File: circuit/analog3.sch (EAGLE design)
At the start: 67 parts, among them IC1 OP07C, IC2 74HC4052D, IC3 AD8603UJ, IC4 AD8221R, IC5 AD8221R, IC6 AD8532ARZ

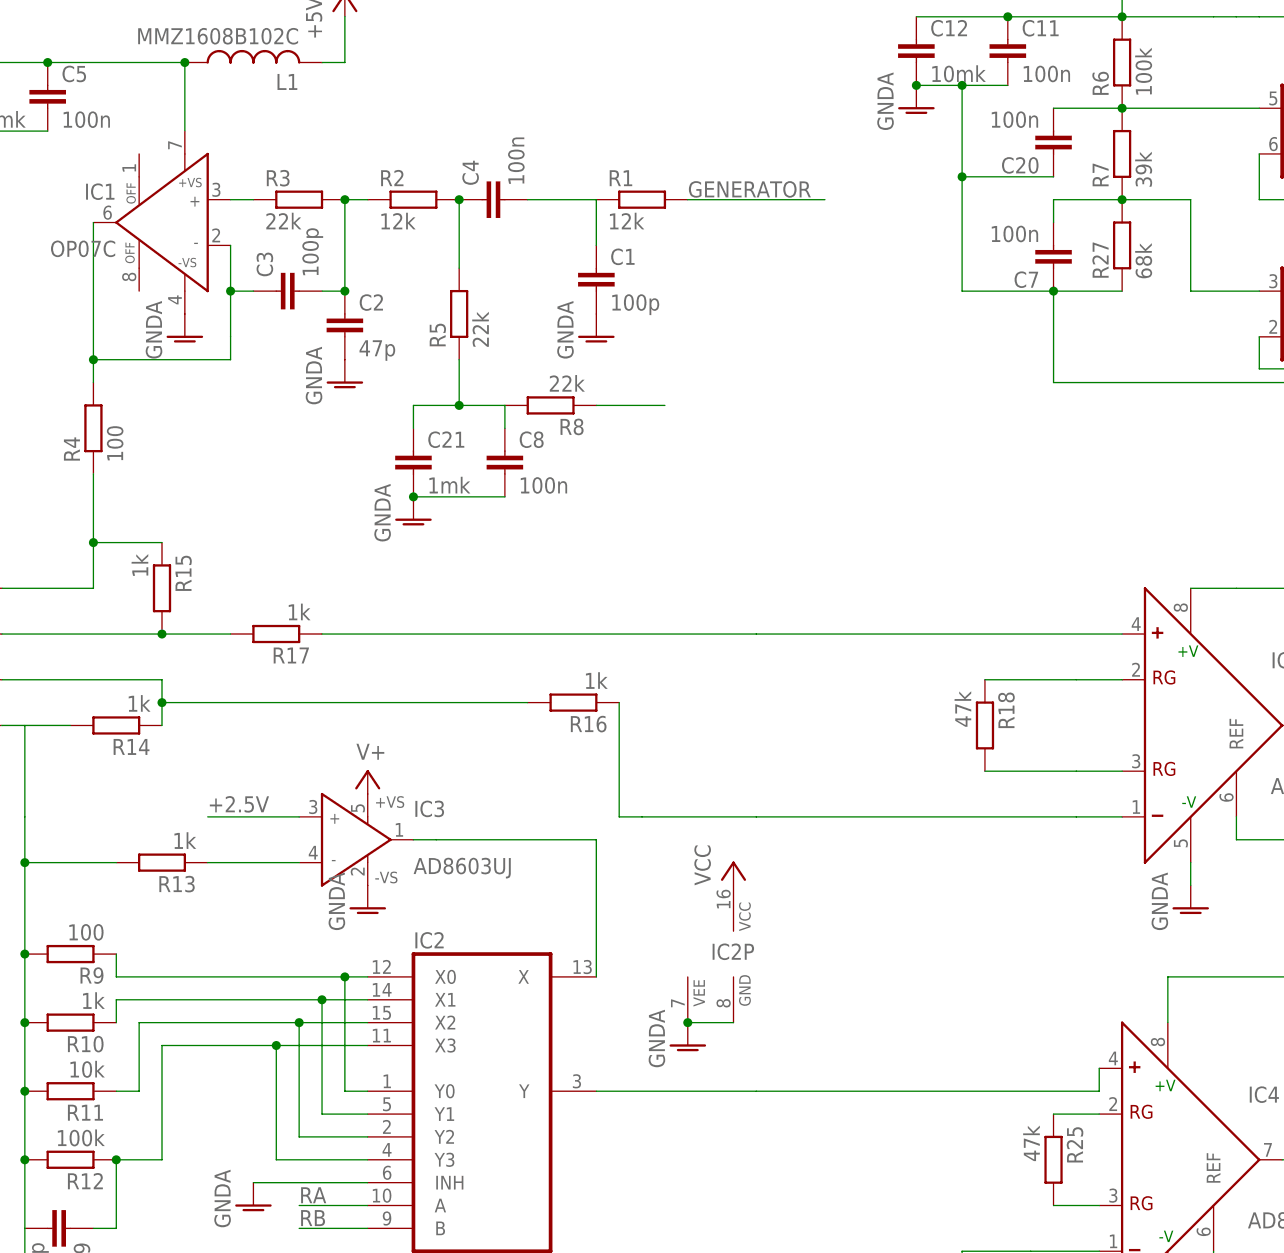
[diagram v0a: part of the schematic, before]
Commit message: - добавили делитель на генератор
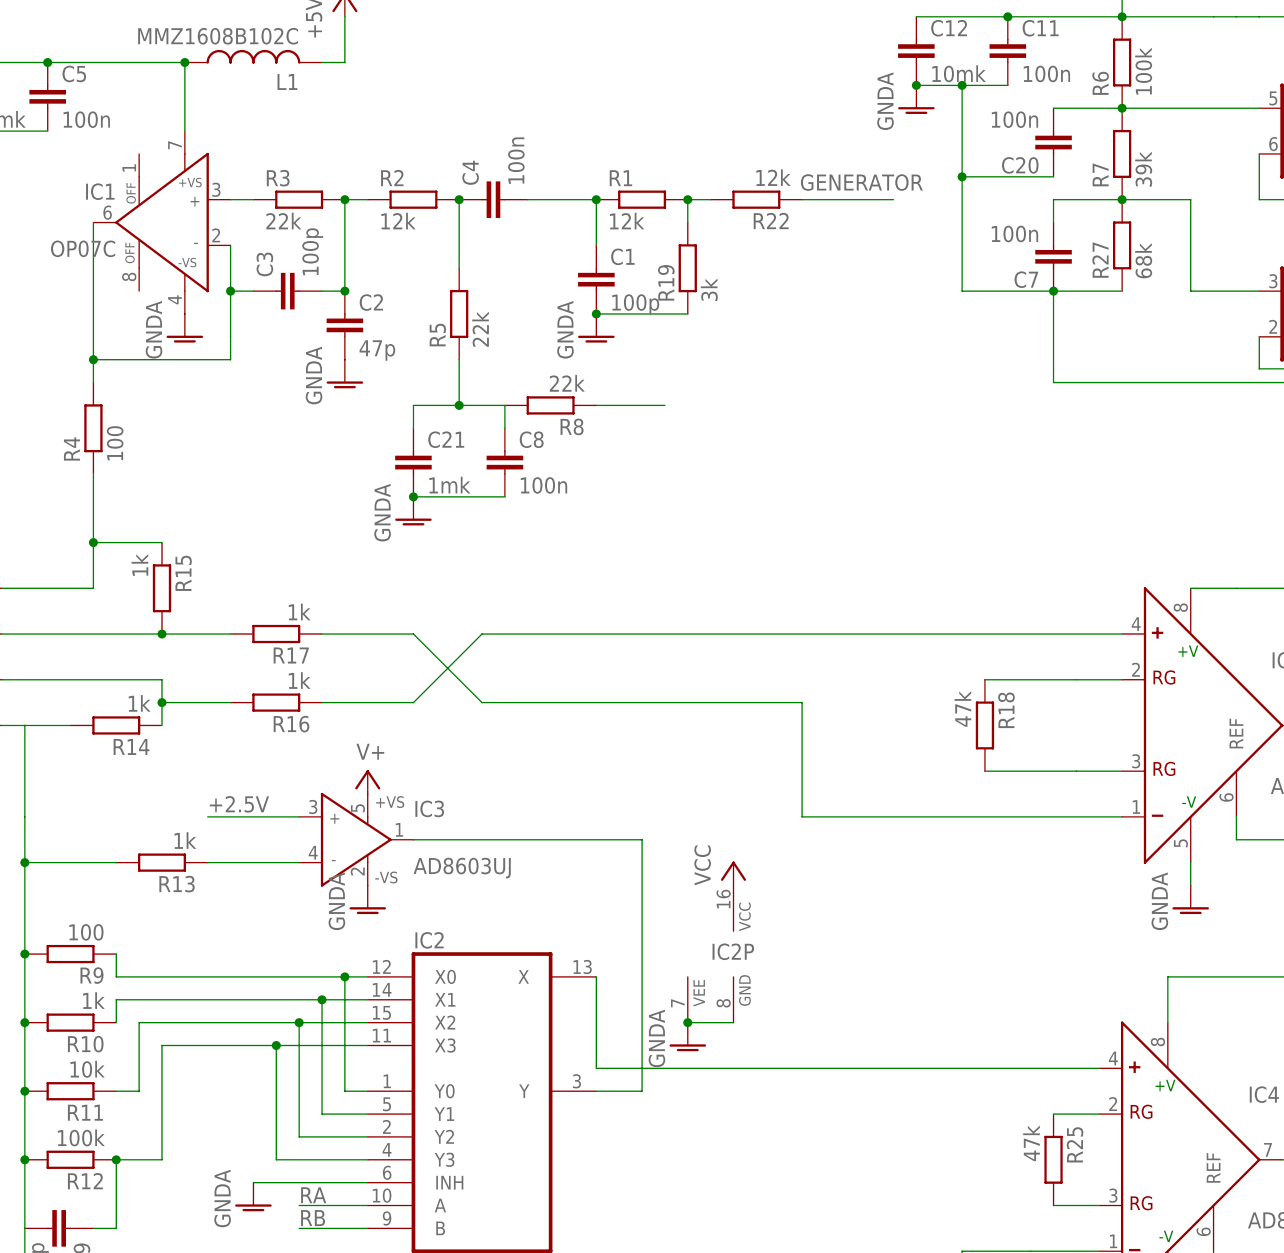
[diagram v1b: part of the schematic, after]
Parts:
- added R19: 3k, rcl:R-EU_R0603
- added R22: 12k, rcl:R-EU_R0603
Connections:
- removed net V_IN+: IC5.-, R16.1
- new net N$32: IC5.+, R16.1
- new net N$34: R1.2, R19.2, R22.2
- net GENERATOR: now also R22.1; no longer R1.2
- net GNDA: now also R19.1
- net N$1: now also IC5.-; no longer IC5.+
- net N$11: now also IC2A.Y; no longer IC2A.X
- net N$30: now also IC2A.X; no longer IC2A.Y
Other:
- moved on the sheet: R16
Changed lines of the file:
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@@
 <part name="IC3" library="analog-devices" deviceset="AD8603" device="UJ"/>
 <part name="SUPPLY5" library="supply2" deviceset="V+" device=""/>
+<part name="R19" library="rcl" deviceset="R-EU_" device="R0603" value="3k"/>
+<part name="R22" library="rcl" deviceset="R-EU_" device="R0603" value="12k"/>
 </parts>
 <sheets>
@@
 <instance part="R14" gate="G$1" x="-48.26" y="20.32" rot="R180"/>
 <instance part="R15" gate="G$1" x="-43.18" y="35.56" rot="R270"/>
-<instance part="R16" gate="G$1" x="2.54" y="22.86" rot="R180"/>
+<instance part="R16" gate="G$1" x="-30.48" y="22.86" rot="R180"/>
 <instance part="R17" gate="G$1" x="-30.48" y="30.48" rot="R180"/>
 <instance part="GND8" gate="1" x="71.12" y="0"/>
@@
 <instance part="IC3" gate="G$1" x="-22.86" y="7.62"/>
 <instance part="SUPPLY5" gate="1" x="-20.32" y="15.24"/>
+<instance part="R19" gate="G$1" x="15.24" y="71.12" rot="R90"/>
+<instance part="R22" gate="G$1" x="22.86" y="78.74" rot="R180"/>
 </instances>
 <busses>
@@
 <pinref part="C4" gate="G$1" pin="2"/>
 <wire x1="5.08" y1="78.74" x2="-2.54" y2="78.74" width="0.1524" layer="91"/>
+<junction x="5.08" y="78.74"/>
 </segment>
 </net>
@@
 <net name="GENERATOR" class="0">
 <segment>
-<pinref part="R1" gate="G$1" pin="2"/>
-<wire x1="15.24" y1="78.74" x2="30.48" y2="78.74" width="0.1524" layer="91"/>
-<label x="15.24" y="78.994" size="1.778" layer="95"/>
-</segment>
-<segment>
 <pinref part="X8" gate="-1" pin="1"/>
 <wire x1="170.18" y1="93.98" x2="160.02" y2="93.98" width="0.1524" layer="91"/>
 <label x="154.686" y="94.488" size="1.778" layer="95"/>
+</segment>
+<segment>
+<pinref part="R22" gate="G$1" pin="1"/>
+<wire x1="27.94" y1="78.74" x2="38.1" y2="78.74" width="0.1524" layer="91"/>
+<label x="27.686" y="79.756" size="1.778" layer="95"/>
 </segment>
 </net>
@@
 <pinref part="C1" gate="G$1" pin="2"/>
 <pinref part="GND1" gate="1" pin="GNDA"/>
+<pinref part="R19" gate="G$1" pin="1"/>
+<wire x1="15.24" y1="66.04" x2="5.08" y2="66.04" width="0.1524" layer="91"/>
+<junction x="5.08" y="66.04"/>
 </segment>
 <segment>
@@
 <pinref part="P+6" gate="VCC" pin="VCC"/>
 <pinref part="IC2" gate="P" pin="VCC"/>
-</segment>
-</net>
-<net name="N$11" class="0">
-<segment>
-<pinref part="IC2" gate="A" pin="X"/>
-<wire x1="5.08" y1="7.62" x2="5.08" y2="-7.62" width="0.1524" layer="91"/>
-<wire x1="5.08" y1="7.62" x2="-12.7" y2="7.62" width="0.1524" layer="91"/>
-<pinref part="IC3" gate="G$1" pin="OUT"/>
-<wire x1="-12.7" y1="7.62" x2="-15.24" y2="7.62" width="0.1524" layer="91"/>
 </segment>
 </net>
@@
 <pinref part="R16" gate="G$1" pin="2"/>
 <wire x1="-43.18" y1="22.86" x2="-43.18" y2="20.32" width="0.1524" layer="91"/>
-<wire x1="-2.54" y1="22.86" x2="-43.18" y2="22.86" width="0.1524" layer="91"/>
+<wire x1="-35.56" y1="22.86" x2="-43.18" y2="22.86" width="0.1524" layer="91"/>
 <junction x="-43.18" y="22.86"/>
 </segment>
@@
 <wire x1="83.82" y1="17.78" x2="86.36" y2="17.78" width="0.1524" layer="91"/>
 <wire x1="86.36" y1="17.78" x2="88.9" y2="17.78" width="0.1524" layer="91"/>
-</segment>
-</net>
-<net name="V_IN+" class="0">
-<segment>
-<wire x1="58.42" y1="10.16" x2="22.86" y2="10.16" width="0.1524" layer="91"/>
-<pinref part="R16" gate="G$1" pin="1"/>
-<wire x1="22.86" y1="10.16" x2="10.16" y2="10.16" width="0.1524" layer="91"/>
-<wire x1="10.16" y1="10.16" x2="7.62" y2="10.16" width="0.1524" layer="91"/>
-<wire x1="7.62" y1="10.16" x2="7.62" y2="22.86" width="0.1524" layer="91"/>
-<pinref part="IC5" gate="G$1" pin="-"/>
-<wire x1="63.5" y1="10.16" x2="58.42" y2="10.16" width="0.1524" layer="91"/>
 </segment>
 </net>
@@
 </segment>
 </net>
-<net name="N$1" class="0">
-<segment>
-<pinref part="IC5" gate="G$1" pin="+"/>
-<pinref part="R17" gate="G$1" pin="1"/>
-<wire x1="63.5" y1="30.48" x2="22.86" y2="30.48" width="0.1524" layer="91"/>
-<wire x1="22.86" y1="30.48" x2="-25.4" y2="30.48" width="0.1524" layer="91"/>
-</segment>
-</net>
 <net name="N$9" class="0">
 <segment>
@@
 <pinref part="IC4" gate="G$1" pin="-"/>
 <wire x1="53.34" y1="-38.1" x2="60.96" y2="-38.1" width="0.1524" layer="91"/>
-</segment>
-</net>
-<net name="N$30" class="0">
-<segment>
-<pinref part="IC2" gate="A" pin="Y"/>
-<pinref part="IC4" gate="G$1" pin="+"/>
-<wire x1="5.08" y1="-20.32" x2="22.86" y2="-20.32" width="0.1524" layer="91"/>
-<wire x1="22.86" y1="-20.32" x2="60.96" y2="-20.32" width="0.1524" layer="91"/>
-<wire x1="60.96" y1="-20.32" x2="60.96" y2="-17.78" width="0.1524" layer="91"/>
 </segment>
 </net>
@@
 </segment>
 </net>
+<net name="N$11" class="0">
+<segment>
+<pinref part="IC3" gate="G$1" pin="OUT"/>
+<wire x1="-15.24" y1="7.62" x2="10.16" y2="7.62" width="0.1524" layer="91"/>
+<wire x1="10.16" y1="7.62" x2="10.16" y2="-20.32" width="0.1524" layer="91"/>
+<pinref part="IC2" gate="A" pin="Y"/>
+<wire x1="10.16" y1="-20.32" x2="5.08" y2="-20.32" width="0.1524" layer="91"/>
+</segment>
+</net>
+<net name="N$30" class="0">
+<segment>
+<pinref part="IC4" gate="G$1" pin="+"/>
+<pinref part="IC2" gate="A" pin="X"/>
+<wire x1="60.96" y1="-17.78" x2="5.08" y2="-17.78" width="0.1524" layer="91"/>
+<wire x1="5.08" y1="-17.78" x2="5.08" y2="-7.62" width="0.1524" layer="91"/>
+</segment>
+</net>
+<net name="N$1" class="0">
+<segment>
+<pinref part="IC5" gate="G$1" pin="-"/>
+<wire x1="63.5" y1="10.16" x2="27.94" y2="10.16" width="0.1524" layer="91"/>
+<wire x1="27.94" y1="10.16" x2="27.94" y2="22.86" width="0.1524" layer="91"/>
+<wire x1="27.94" y1="22.86" x2="-7.62" y2="22.86" width="0.1524" layer="91"/>
+<wire x1="-7.62" y1="22.86" x2="-15.24" y2="30.48" width="0.1524" layer="91"/>
+<pinref part="R17" gate="G$1" pin="1"/>
+<wire x1="-15.24" y1="30.48" x2="-25.4" y2="30.48" width="0.1524" layer="91"/>
+</segment>
+</net>
+<net name="N$32" class="0">
+<segment>
+<pinref part="IC5" gate="G$1" pin="+"/>
+<wire x1="63.5" y1="30.48" x2="-7.62" y2="30.48" width="0.1524" layer="91"/>
+<wire x1="-7.62" y1="30.48" x2="-15.24" y2="22.86" width="0.1524" layer="91"/>
+<pinref part="R16" gate="G$1" pin="1"/>
+<wire x1="-15.24" y1="22.86" x2="-25.4" y2="22.86" width="0.1524" layer="91"/>
+</segment>
+</net>
+<net name="N$34" class="0">
+<segment>
+<pinref part="R19" gate="G$1" pin="2"/>
+<pinref part="R1" gate="G$1" pin="2"/>
+<wire x1="15.24" y1="76.2" x2="15.24" y2="78.74" width="0.1524" layer="91"/>
+<pinref part="R22" gate="G$1" pin="2"/>
+<wire x1="17.78" y1="78.74" x2="15.24" y2="78.74" width="0.1524" layer="91"/>
+<junction x="15.24" y="78.74"/>
+</segment>
+</net>
